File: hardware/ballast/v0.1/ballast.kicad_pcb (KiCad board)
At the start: 4 copper layers, 24 parts, among them J1 DALI, Q1 NX138BKR, U1 ICE40UP5K-SG48ITR, U2 SPI-Flash_EP, U3 140357145300, U4 140357145300

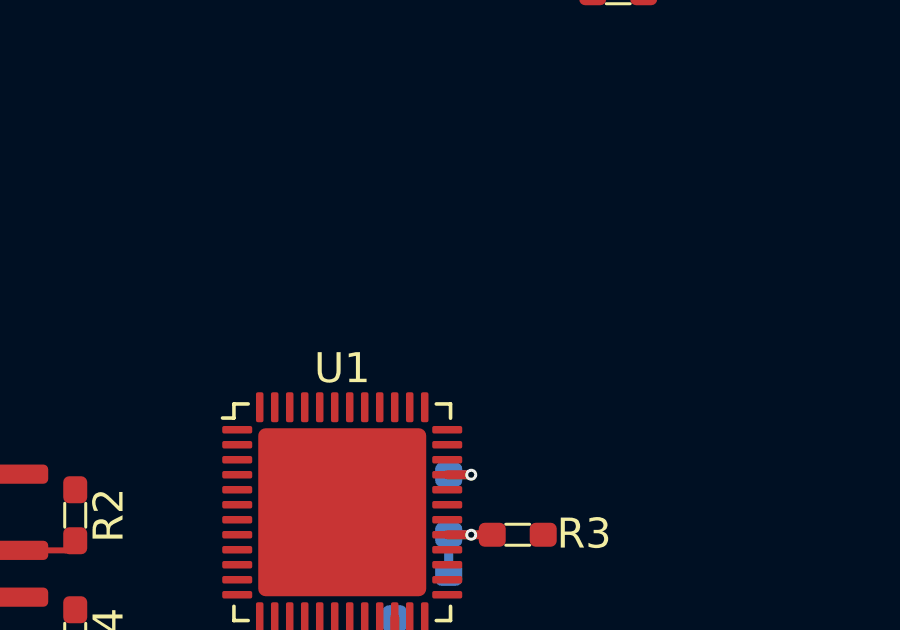
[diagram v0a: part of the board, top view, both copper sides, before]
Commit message: Added the FRAM for persisting DALI config to the board
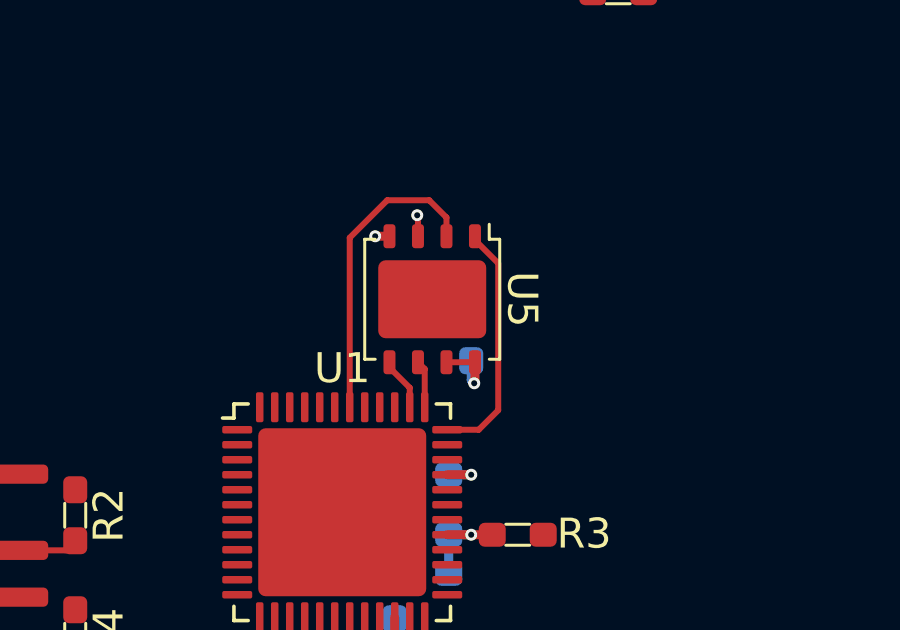
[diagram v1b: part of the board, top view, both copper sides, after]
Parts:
- added C12: 0.1uF, rhais_rcl:C0603, B.Cu at (154.2, 104.0)
- added U5: FM25L16B, rhais_package-qfn:WDFN-8-1EP_4x4.5mm_P0.95mm_EP2.6x3.6mm, F.Cu at (152.9, 102.8)
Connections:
- U1 pad 36: unconnected-(U1-Pad36) -> /~{FRAM_CS}
- U1 pad 37: unconnected-(U1-Pad37) -> /FRAM_SCLK
- U1 pad 38: unconnected-(U1-Pad38) -> /FRAM_COPI
- U1 pad 42: unconnected-(U1-Pad42) -> /FRAM_CIPO
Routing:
- net /FRAM_CIPO: track 0.00 -> 10.3 mm
- net /~{FRAM_CS}: track 0.00 -> 8.09 mm
- net +3V3: track 3.10 -> 6.26 mm, vias 2 -> 4
- net /FRAM_COPI: track 0.00 -> 1.78 mm
- net /FRAM_SCLK: track 0.00 -> 1.59 mm
- net GND: track 0.00 -> 0.47 mm, vias 0 -> 1
